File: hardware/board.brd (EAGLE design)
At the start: 100 x 100 mm, 79 parts, among them CON1 USB-FPGA1.11, IC1 AD80XX

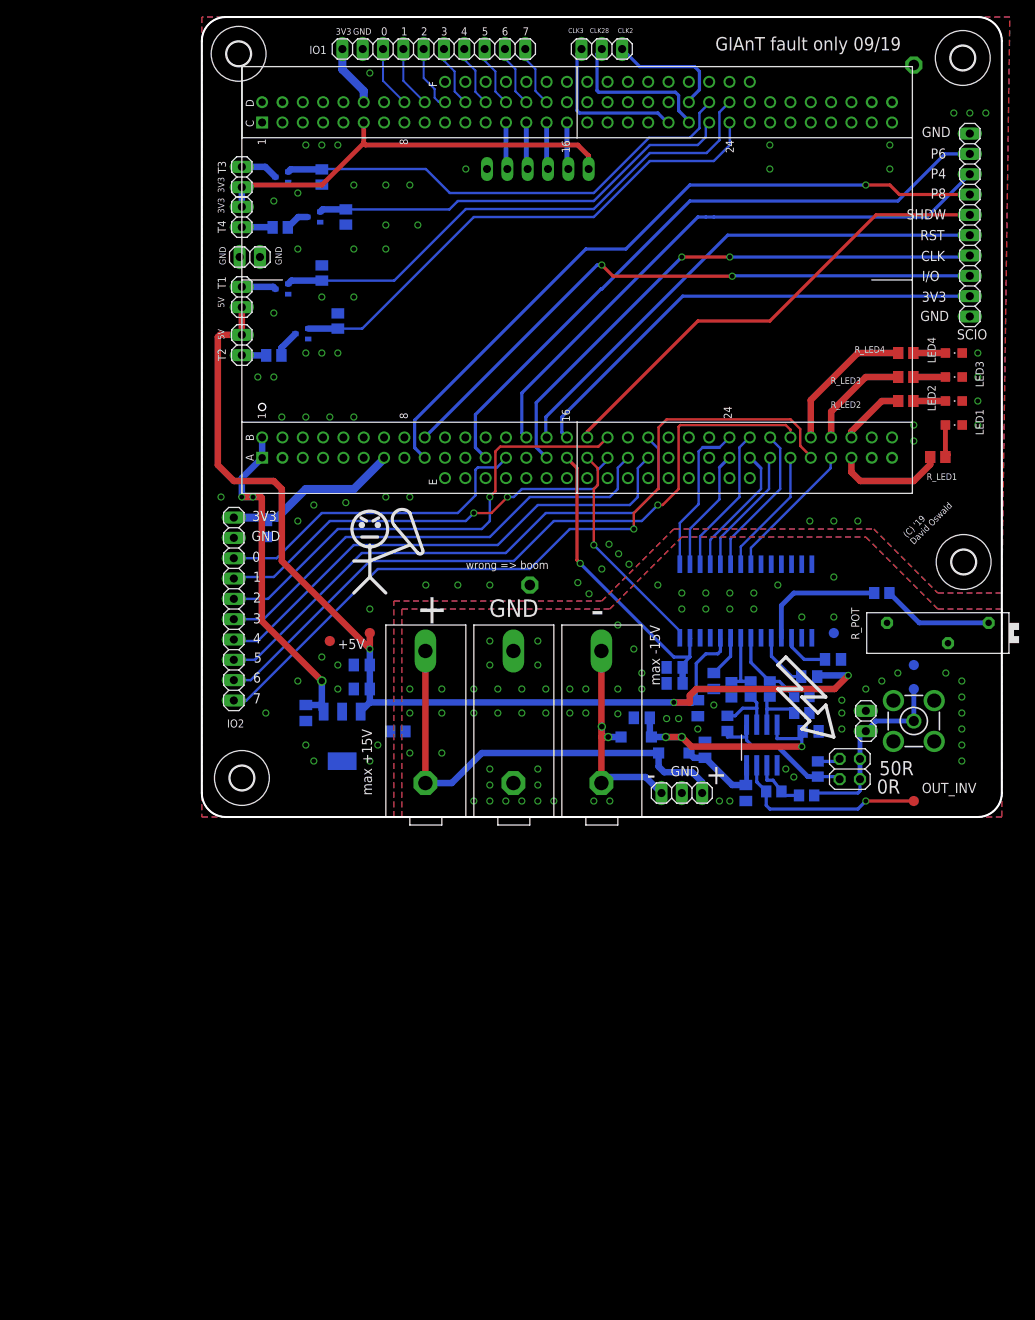
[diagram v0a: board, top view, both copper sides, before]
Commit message: Working on improved board revB Added DC-DC and selection jumper Added some libraries Fixed THS3062 symbol Split up sheets
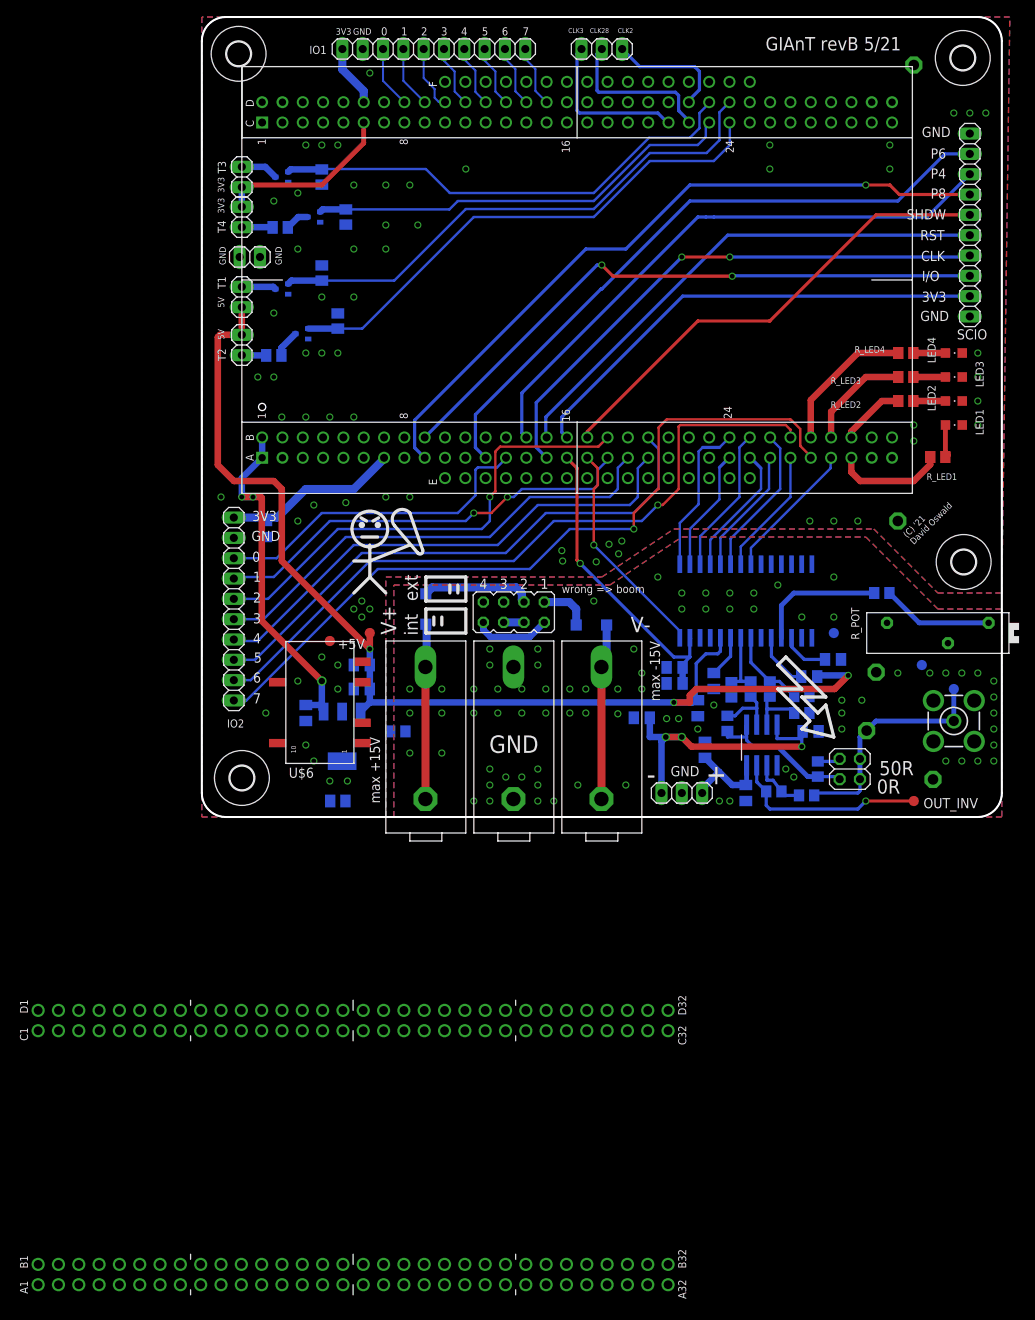
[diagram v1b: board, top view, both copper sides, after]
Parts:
- removed CON_UC: (no value), con-molex:22-23-2061
- added CON2: USB-FPGA-2THT, usb-fpga-2:USB-FPGA-2-THT
- added R7: 0R, rcl:M0805
- added TP2, TP3, TP_GND2: TPPAD1-13, testpad:P1-13
- added U$6: IAS0105D09, xppower-IAS01:SMD-DIP10
- IC1: value AD80XX -> THS3062; device ad80xx:SO08 -> ths3062:SO08
- JP1: device pinhead:1X02 -> jumper:JP4Q
- moved TP_GNDA 46.7 mm to (87.0, 37.0)
- moved JP1 46.1 mm to (39.0, 25.6), turned to 180 degrees
- moved D2 35.8 mm to (28.0, 26.0), turned to 270 degrees
- moved D1 15.1 mm to (48.7, 24.0), turned to 0 degrees
- moved DAC_OUT 5.00 mm to (94.0, 12.0)
- moved TP_OUT 5.00 mm to (94.0, 16.0)
- moved CN+ 2.00 mm to (34.0, 22.0)
- moved CN- 2.00 mm to (56.0, 22.0)
- moved CNG 2.00 mm to (45.0, 22.0)
- moved TP_GND1 1.00 mm to (90.0, 19.0)
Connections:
- removed net N$60: CON1.C13, CON_UC.5
- removed net N$61: CON1.C14, CON_UC.4
- removed net N$62: CON1.C15, CON_UC.3
- removed net N$63: CON1.C16, CON_UC.2
- new net +9V: JP1.5, U$6.P$7
- new net -9V: JP1.7, U$6.P$5
- new net N$13: D2.C, JP1.3
- new net N$17: D1.A, JP1.1
- new net N$7: R7.1, U$6.P$4
- net +5V: now also U$6.P$2
- net +5V/3: no longer CON_UC.1
- net DAC_OUT_NET: now also TP2.TP; no longer JP1.1
- net GND: now also U$6.P$1; no longer CON_UC.6
- net GND1: now also R7.2, TP3.TP, TP_GND2.TP; no longer JP1.2
- net V+: no longer OP_VCC.3
- net V-: no longer OP_VCC.1
- net VCC+: now also JP1.4, JP1.6, OP_VCC.3; no longer D2.C
- net VCC-: now also JP1.2, JP1.8, OP_VCC.1; no longer D1.A
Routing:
- net V+: track 56.5 -> 22.0 mm
- net +5V/3: track 53.0 -> 22.6 mm
- net VCC-: track 30.8 -> 47.7 mm
- net N$13: track 0.00 -> 13.9 mm
- net V-: track 29.7 -> 22.0 mm, vias 2 -> 0
- net N$17: track 0.00 -> 6.35 mm
- net N$63: track 5.89 -> 0.00 mm
- net N$62: track 5.89 -> 0.00 mm
- net N$61: track 5.89 -> 0.00 mm
- net N$60: track 5.89 -> 0.00 mm
- net DAC_OUT_NET: track 24.2 -> 29.3 mm
- net VCC+: track 11.3 -> 15.1 mm
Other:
- board text added: "(C) '21 David Oswald"
- board text added: "GIAnT revB 5/21"
- board text added: "V+"
- board text added: "V-"
- board text added: "ext"
- board text added: "int"
- board text removed: "(C) '19 David Oswald"
- board text removed: "GIAnT fault only 09/19"

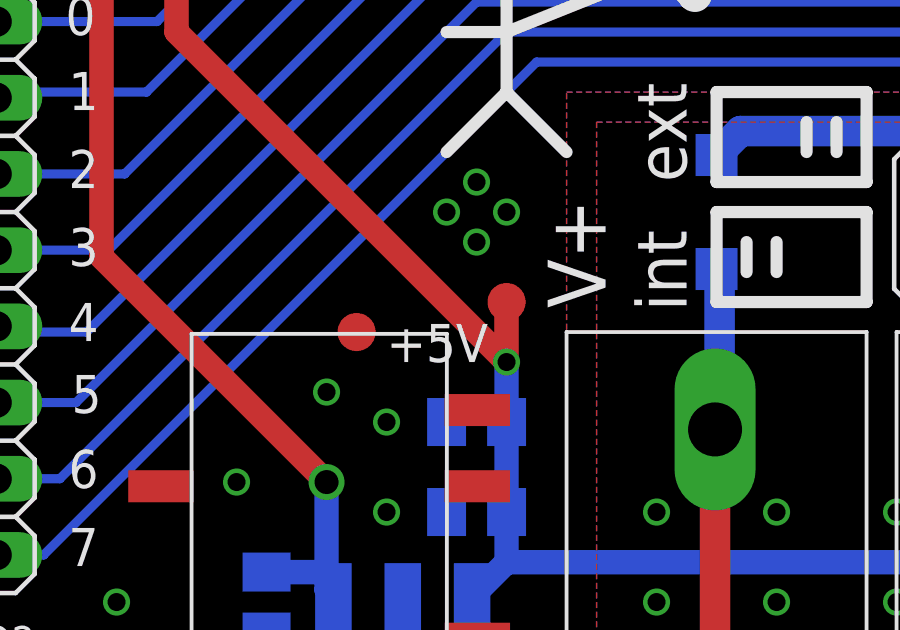
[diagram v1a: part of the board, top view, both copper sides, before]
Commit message: Working on change to new v2 pinout
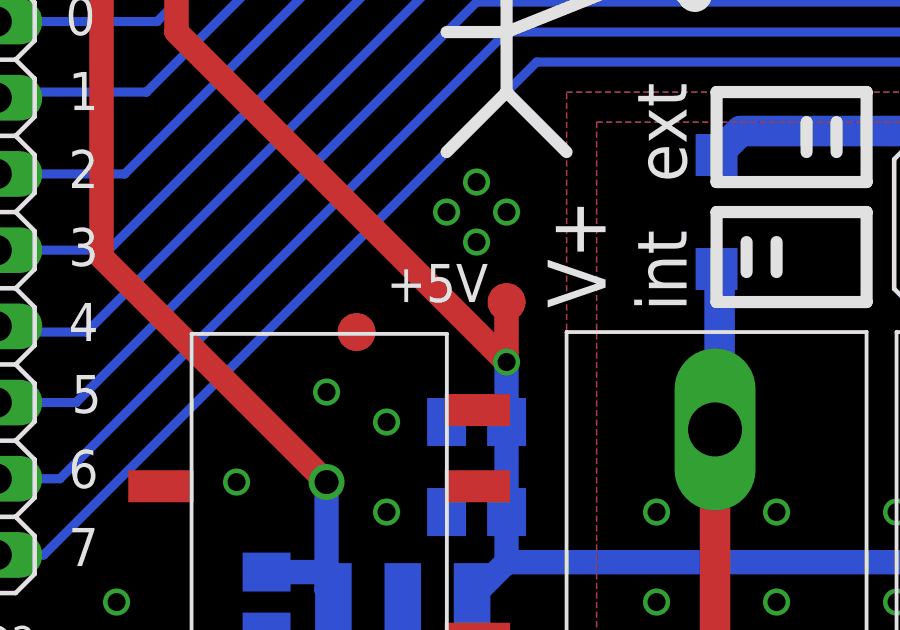
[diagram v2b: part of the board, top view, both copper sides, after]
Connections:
- net N$1 renamed GPIO2_0
- net N$2 renamed GPIO2_1
- net N$3 renamed GPIO2_2
- net N$4 renamed GPIO2_3
- net N$5 renamed GPIO2_4
- net N$6 renamed GPIO2_5
- net N$8 renamed GPIO2_6
- net N$9 renamed GPIO2_7
- removed net CLK: AD9708.28, CON1.A17
- removed net N$25: CON1.D8, GPIO.3
- removed net N$26: CON1.D9, GPIO.4
- removed net N$27: CON1.D10, GPIO.5
- removed net N$28: CON1.D11, GPIO.6
- removed net N$29: CON1.D12, GPIO.7
- removed net N$30: CON1.D13, GPIO.8
- removed net N$31: CON1.D14, GPIO.9
- removed net N$32: CON1.D15, GPIO.10
- removed net N$53: CON1.B30, R_LED2.2
- removed net N$54: CON1.A30, R_LED1.2
- removed net N$55: CON1.B29, R_LED3.2
- removed net N$56: CON1.B28, R_LED4.2
- new net DAC_CLK: AD9708.28, CON1.A17, CON2.B11
- new net GPIO0: CON1.D8, CON2.D3, GPIO.3
- new net GPIO1: CON1.D9, CON2.D4, GPIO.4
- new net GPIO2: CON1.D10, CON2.D5, GPIO.5
- new net GPIO3: CON1.D11, CON2.D7, GPIO.6
- new net GPIO4: CON1.D12, CON2.C8, GPIO.7
- new net GPIO5: CON1.D13, CON2.C10, GPIO.8
- new net GPIO6: CON1.D14, CON2.D11, GPIO.9
- new net GPIO7: CON1.D15, CON2.C13, GPIO.10
- new net LED1_PIN: CON1.A30, CON2.A30, R_LED1.2
- new net LED2_PIN: CON1.B30, CON2.B30, R_LED2.2
- new net LED3_PIN: CON1.B29, CON2.B29, R_LED3.2
- new net LED4_PIN: CON1.B28, CON2.B28, R_LED4.2
- net +5V/1: now also CON2.A15
- net +5V/2: now also CON2.D18
- net +5V/3: now also CON2.C18
- net CLK_SC: now also CON2.B9
- net DB0: now also CON2.A29
- net DB1: now also CON2.B26
- net DB2: now also CON2.B25
- net DB3: now also CON2.A25
- net DB4: now also CON2.B23
- net DB5: now also CON2.A24
- net DB6: now also CON2.A22
- net DB7: now also CON2.B22
- net GCLK2: now also CON2.D24
- net GCLK28: now also CON2.C24
- net GCLK3: now also CON2.D22
- net GND: now also CON2.A16, CON2.A2, CON2.B16, CON2.B2, CON2.B32, CON2.C17, CON2.C2, CON2.C32, CON2.D17, CON2.D2, CON2.D32
- net IO: now also CON2.B5
- net PIN4: now also CON2.B8
- net PIN6: now also CON2.A6
- net PIN8: now also CON2.A5
- net RST: now also CON2.A10
- net SHDN: now also CON2.A12
- net SW1: now also CON2.B6
- net SW2: now also CON2.A8
- net T1: now also CON2.D27
- net T2: now also CON2.C27
- net T3: now also CON2.C26
- net T4: now also CON2.D25
- net VEE: now also CON2.A1, CON2.B1
- net VPP: now also CON2.B15
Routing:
- net DAC_CLK: track 0.00 -> 27.7 mm, vias 0 -> 1
- net CLK: track 27.7 -> 0.00 mm, vias 1 -> 0
- net N$56: track 18.0 -> 0.00 mm
- net LED4_PIN: track 0.00 -> 18.0 mm
- net N$54: track 13.9 -> 0.00 mm
- net LED1_PIN: track 0.00 -> 13.9 mm
- net N$55: track 13.4 -> 0.00 mm
- net LED3_PIN: track 0.00 -> 13.4 mm
- net N$27: track 8.19 -> 0.00 mm
- net GPIO2: track 0.00 -> 8.19 mm
- net N$53: track 8.18 -> 0.00 mm
- net LED2_PIN: track 0.00 -> 8.18 mm
- net N$30: track 7.75 -> 0.00 mm
- net GPIO5: track 0.00 -> 7.75 mm
- net N$32: track 7.75 -> 0.00 mm
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
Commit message: Added all v2 pins and labels
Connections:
- net GPIO0: now also CON2.C6; no longer CON2.D3
- net GPIO1: now also CON2.D6; no longer CON2.D4
- net GPIO2: now also CON2.C7; no longer CON2.D5
- net GPIO2_0: now also CON2.B12
- net GPIO2_1: now also CON2.A13
- net GPIO2_2: now also CON2.B13
- net GPIO2_3: now also CON2.B14
- net GPIO2_4: now also CON2.A19
- net GPIO2_5: now also CON2.B19
- net GPIO2_6: now also CON2.A20
- net GPIO2_7: now also CON2.B20
- net IO: now also CON2.A9; no longer CON2.B5
- net PIN8: now also CON2.A7; no longer CON2.A5
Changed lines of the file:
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@@
 <wire x1="22.65" y1="96" x2="22.65" y2="92.025" width="0.254" layer="16"/>
 <wire x1="22.65" y1="92.025" x2="25.32" y2="89.355" width="0.254" layer="16"/>
-<contactref element="CON2" pad="D3"/>
-<wire x1="-15.38" y1="-24.17" x2="25.32" y2="89.355" width="0" layer="19" extent="1-1"/>
+<contactref element="CON2" pad="C6"/>
+<wire x1="-7.76" y1="-26.71" x2="25.32" y2="89.355" width="0" layer="19" extent="1-1"/>
 </signal>
 <signal name="GPIO1">
@@
 <wire x1="25.19" y1="96" x2="25.19" y2="92.025" width="0.254" layer="16"/>
 <wire x1="25.19" y1="92.025" x2="27.86" y2="89.355" width="0.254" layer="16"/>
-<contactref element="CON2" pad="D4"/>
-<wire x1="-12.84" y1="-24.17" x2="27.86" y2="89.355" width="0" layer="19" extent="1-1"/>
+<contactref element="CON2" pad="D6"/>
+<wire x1="-7.76" y1="-24.17" x2="27.86" y2="89.355" width="0" layer="19" extent="1-1"/>
 </signal>
 <signal name="GPIO2">
@@
 <wire x1="29.6" y1="89.4" x2="30.355" y2="89.4" width="0.254" layer="16"/>
 <wire x1="30.355" y1="89.4" x2="30.4" y2="89.355" width="0.254" layer="16"/>
-<contactref element="CON2" pad="D5"/>
-<wire x1="-10.3" y1="-24.17" x2="29.6" y2="89.4" width="0" layer="19" extent="16-16"/>
+<contactref element="CON2" pad="C7"/>
+<wire x1="-5.22" y1="-26.71" x2="29.6" y2="89.4" width="0" layer="19" extent="16-16"/>
 </signal>
 <signal name="V+">
@@
 <wire x1="53" y1="71" x2="61" y2="79" width="0.4064" layer="16"/>
 <wire x1="61" y1="79" x2="83" y2="79" width="0.4064" layer="16"/>
-<contactref element="CON2" pad="A5"/>
-<wire x1="-10.3" y1="-58.46" x2="27.86" y2="44.905" width="0" layer="19" extent="1-1"/>
+<contactref element="CON2" pad="A7"/>
+<wire x1="-5.22" y1="-58.46" x2="27.86" y2="44.905" width="0" layer="19" extent="1-1"/>
 </signal>
 <signal name="IO">
@@
 <via x="50" y="69" extent="1-16" drill="0.6" shape="octagon"/>
 <wire x1="50" y1="69" x2="49.415" y2="69" width="0.4064" layer="16"/>
-<contactref element="CON2" pad="B5"/>
-<wire x1="-10.3" y1="-55.92" x2="27.86" y2="47.445" width="0" layer="19" extent="1-1"/>
+<contactref element="CON2" pad="A9"/>
+<wire x1="-0.14" y1="-58.46" x2="27.86" y2="47.445" width="0" layer="19" extent="1-1"/>
 </signal>
 <signal name="PIN6">
@@
 <wire x1="32" y1="38" x2="34.2" y2="40.2" width="0.3048" layer="16"/>
 <wire x1="15" y1="38" x2="32" y2="38" width="0.3048" layer="16"/>
+<contactref element="CON2" pad="B12"/>
+<wire x1="9.35" y1="32.35" x2="7.48" y2="-55.92" width="0" layer="19" extent="16-16"/>
 </signal>
 <signal name="GPIO2_1">
@@
 <wire x1="39" y1="40" x2="40" y2="41" width="0.3048" layer="16"/>
 <wire x1="40" y1="41" x2="49" y2="41" width="0.3048" layer="16"/>
+<contactref element="CON2" pad="A13"/>
+<wire x1="9" y1="30" x2="10.02" y2="-58.46" width="0" layer="19" extent="16-16"/>
 </signal>
 <signal name="GPIO2_2">
@@
 <wire x1="17" y1="36" x2="35" y2="36" width="0.3048" layer="16"/>
 <wire x1="35" y1="36" x2="36" y2="37" width="0.3048" layer="16"/>
+<contactref element="CON2" pad="B13"/>
+<wire x1="8.27" y1="27.27" x2="10.02" y2="-55.92" width="0" layer="19" extent="16-16"/>
 </signal>
 <signal name="GPIO2_3">
@@
 <wire x1="36" y1="35" x2="41" y2="40" width="0.3048" layer="16"/>
 <wire x1="41" y1="40" x2="51" y2="40" width="0.3048" layer="16"/>
+<contactref element="CON2" pad="B14"/>
+<wire x1="7.73" y1="24.73" x2="12.56" y2="-55.92" width="0" layer="19" extent="16-16"/>
 </signal>
 <signal name="GPIO2_4">
@@
 <wire x1="7" y1="22" x2="4.19" y2="22" width="0.3048" layer="16"/>
 <wire x1="4.19" y1="22" x2="4" y2="22.19" width="0.3048" layer="16"/>
+<contactref element="CON2" pad="A19"/>
+<wire x1="7" y1="22" x2="25.26" y2="-58.46" width="0" layer="19" extent="16-16"/>
 </signal>
 <signal name="GPIO2_5">
@@
 <wire x1="55.8" y1="47.3" x2="57.1" y2="46" width="0.3048" layer="16"/>
 <wire x1="57.1" y1="46" x2="57.1" y2="41.1" width="0.3048" layer="16"/>
+<contactref element="CON2" pad="B19"/>
+<wire x1="6.65" y1="19.65" x2="25.26" y2="-55.92" width="0" layer="19" extent="16-16"/>
 </signal>
 <signal name="GPIO2_6">
@@
 <wire x1="73" y1="49" x2="59.8" y2="49" width="0.3048" layer="1"/>
 <wire x1="59.8" y1="49" x2="59.6" y2="48.8" width="0.3048" layer="1"/>
+<contactref element="CON2" pad="A20"/>
+<wire x1="6.11" y1="17.11" x2="27.8" y2="-58.46" width="0" layer="19" extent="16-16"/>
 </signal>
 <signal name="GPIO2_7">
@@
 <wire x1="54" y1="38" x2="54" y2="36" width="0.3048" layer="1"/>
 <via x="54" y="36" extent="1-16" drill="0.6" shape="octagon"/>
+<contactref element="CON2" pad="B20"/>
+<wire x1="5.57" y1="14.57" x2="27.8" y2="-55.92" width="0" layer="19" extent="16-16"/>
 </signal>
 <signal name="VCCIO">
-<contactref element="CON1" pad="A7"/>
 <contactref element="GPIO2" pad="1"/>
 <contactref element="C19" pad="1"/>
-<wire x1="22.78" y1="44.905" x2="22.78" y2="44.78" width="1.016" layer="16"/>
 <wire x1="22.78" y1="44.78" x2="19" y2="41" width="1.016" layer="16"/>
 <wire x1="4" y1="37.43" x2="8" y2="37.43" width="1.016" layer="16"/>
@@
 <wire x1="13" y1="41" x2="19" y2="41" width="1.016" layer="16"/>
 <wire x1="8" y1="37" x2="8" y2="37.43" width="1.016" layer="16"/>
+<contactref element="CON1" pad="A7"/>
+<wire x1="22.78" y1="44.78" x2="22.78" y2="44.905" width="0" layer="19" extent="16-16"/>
 </signal>
 <signal name="N$69">
